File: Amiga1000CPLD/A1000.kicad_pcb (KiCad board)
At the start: 2 copper layers, 80 x 81.7 mm, 15 parts, among them J1 Raspberry_Pi_2_3, J2 CSYNC IN, U1 DeniseSocket, U2 DenisePins, U3 XC9572VQ44

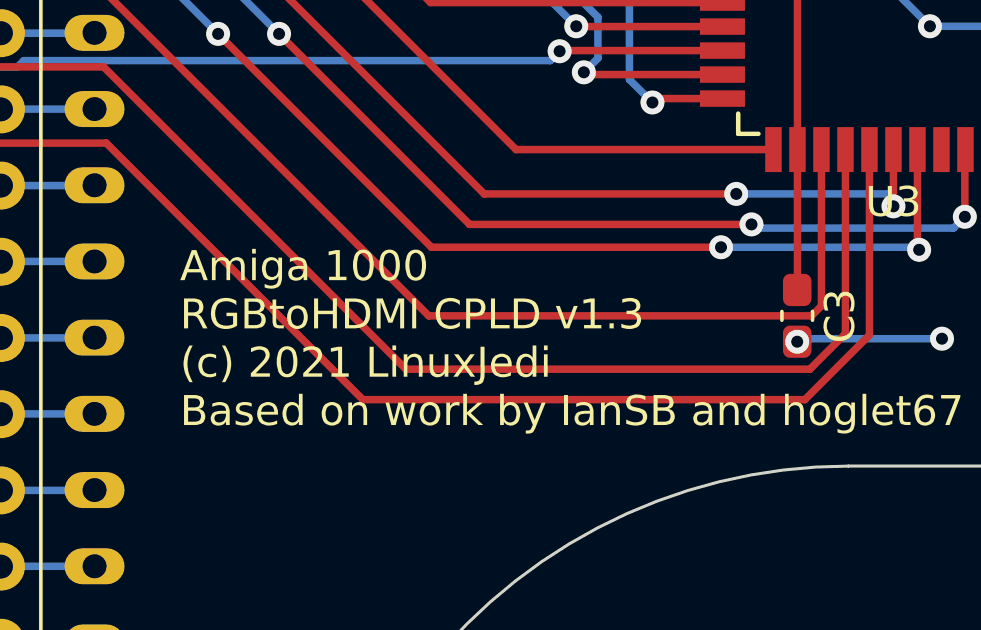
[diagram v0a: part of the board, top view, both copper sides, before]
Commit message: Remove LinuxJedi logo from A1000 board
Fixes #9
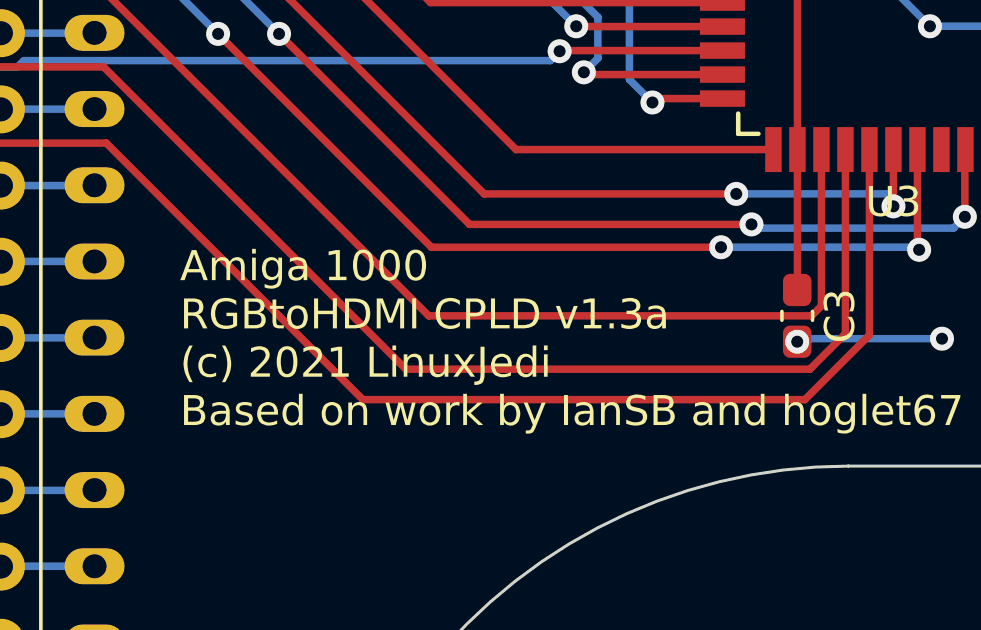
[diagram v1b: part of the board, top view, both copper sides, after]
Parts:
- removed G***: LOGO, lxj:lxj2
- removed G***: LOGO, lxj:lxj
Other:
- board text added: "Amiga 1000 RGBtoHDMI CPLD v1.3a (c) 2021 LinuxJedi Based on work by IanSB and hoglet67"
- board text removed: "Amiga 1000 RGBtoHDMI CPLD v1.3 (c) 2021 LinuxJedi Based on work by IanSB and hoglet67"
